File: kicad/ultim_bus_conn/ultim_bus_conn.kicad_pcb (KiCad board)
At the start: 2 copper layers, 121.9 x 10.2 mm, 16 parts, among them P1 CONN_1, P2 CONN_1, P3 CONN_1, P4 CONN_1, P5 CONN_1, P6 CONN_1, P7 CONN_1, P8 CONN_1

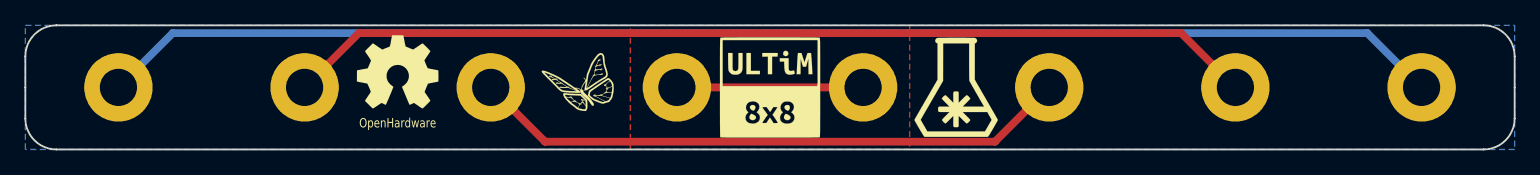
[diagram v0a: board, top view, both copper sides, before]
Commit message: U88 connector strip PCB update
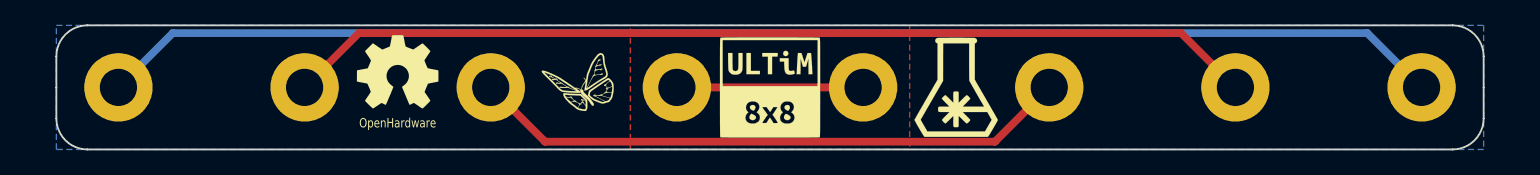
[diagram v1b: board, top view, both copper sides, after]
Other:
- board size 121.9 x 10.2 mm -> 116.8 x 10.2 mm
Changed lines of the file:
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@@
-(kicad_pcb (version 4) (host pcbnew 4.0.6-e0-6349~53~ubuntu16.04.1)
+(kicad_pcb (version 4) (host pcbnew 4.0.7-e0-6372~58~ubuntu16.04.1)
   (general
-    (links 0)
+    (links 4)
     (no_connects 0)
-    (area 43.104999 45.644999 165.175001 55.955001)
+    (area 33.357144 43.7896 162.635001 62.39)
     (thickness 1.6)
     (drawings 12)
@@
     (visible_elements FFFFFF7F)
     (pcbplotparams
-      (layerselection 0x00130_80000001)
-      (usegerberextensions false)
-      (excludeedgelayer false)
+      (layerselection 0x010f0_80000001)
+      (usegerberextensions true)
+      (usegerberattributes true)
+      (excludeedgelayer true)
       (linewidth 0.050800)
-      (plotframeref true)
+      (plotframeref false)
       (viasonmask false)
       (mode 1)
@@
       (plotvalue true)
       (plotinvisibletext false)
-      (padsonsilk true)
-      (subtractmaskfromsilk false)
-      (outputformat 4)
+      (padsonsilk false)
+      (subtractmaskfromsilk true)
+      (outputformat 1)
       (mirror false)
       (drillshape 0)
       (scaleselection 1)
-      (outputdirectory ultim_bus_conn_pdf/))
+      (outputdirectory ultim_bus_conn_gerber/))
   )
   (net 0 "")
@@
     (arrow2b (pts (xy 38.100001 45.72) (xy 38.686422 46.846504)))
   )
-  (dimension 121.92 (width 0.3) (layer Dwgs.User)
-    (gr_text "4.8000 in" (at 104.14 61.039999) (layer Dwgs.User)
+  (dimension 116.84 (width 0.3) (layer Dwgs.User)
+    (gr_text "4.6000 in" (at 104.14 61.039999) (layer Dwgs.User)
       (effects (font (size 1.5 1.5) (thickness 0.3)))
     )
-    (feature1 (pts (xy 165.1 57.15) (xy 165.1 62.389999)))
-    (feature2 (pts (xy 43.18 57.15) (xy 43.18 62.389999)))
-    (crossbar (pts (xy 43.18 59.689999) (xy 165.1 59.689999)))
-    (arrow1a (pts (xy 165.1 59.689999) (xy 163.973496 60.27642)))
-    (arrow1b (pts (xy 165.1 59.689999) (xy 163.973496 59.103578)))
-    (arrow2a (pts (xy 43.18 59.689999) (xy 44.306504 60.27642)))
-    (arrow2b (pts (xy 43.18 59.689999) (xy 44.306504 59.103578)))
-  )
-  (gr_arc (start 162.56 53.34) (end 165.1 53.34) (angle 90) (layer Edge.Cuts) (width 0.15))
-  (gr_arc (start 162.56 48.26) (end 162.56 45.72) (angle 90) (layer Edge.Cuts) (width 0.15))
-  (gr_arc (start 45.72 53.34) (end 45.72 55.88) (angle 90) (layer Edge.Cuts) (width 0.15))
-  (gr_arc (start 45.72 48.26) (end 43.18 48.26) (angle 90) (layer Edge.Cuts) (width 0.15))
-  (gr_line (start 43.18 53.34) (end 43.18 50.8) (layer Edge.Cuts) (width 0.15))
-  (gr_line (start 162.56 55.88) (end 45.72 55.88) (layer Edge.Cuts) (width 0.15))
-  (gr_line (start 165.1 50.8) (end 165.1 53.34) (layer Edge.Cuts) (width 0.15))
-  (gr_line (start 165.1 48.26) (end 165.1 50.8) (layer Edge.Cuts) (width 0.15))
-  (gr_line (start 45.72 45.72) (end 162.56 45.72) (layer Edge.Cuts) (width 0.15))
-  (gr_line (start 43.18 50.8) (end 43.18 48.26) (layer Edge.Cuts) (width 0.15))
+    (feature1 (pts (xy 162.56 57.15) (xy 162.56 62.389999)))
+    (feature2 (pts (xy 45.72 57.15) (xy 45.72 62.389999)))
+    (crossbar (pts (xy 45.72 59.689999) (xy 162.56 59.689999)))
+    (arrow1a (pts (xy 162.56 59.689999) (xy 161.433496 60.27642)))
+    (arrow1b (pts (xy 162.56 59.689999) (xy 161.433496 59.103578)))
+    (arrow2a (pts (xy 45.72 59.689999) (xy 46.846504 60.27642)))
+    (arrow2b (pts (xy 45.72 59.689999) (xy 46.846504 59.103578)))
+  )
+  (gr_arc (start 160.02 53.34) (end 162.56 53.34) (angle 90) (layer Edge.Cuts) (width 0.15))
+  (gr_arc (start 160.02 48.26) (end 160.02 45.72) (angle 90) (layer Edge.Cuts) (width 0.15))
+  (gr_arc (start 48.26 53.34) (end 48.26 55.88) (angle 90) (layer Edge.Cuts) (width 0.15))
+  (gr_arc (start 48.26 48.26) (end 45.72 48.26) (angle 90) (layer Edge.Cuts) (width 0.15))
+  (gr_line (start 45.72 53.34) (end 45.72 50.8) (layer Edge.Cuts) (width 0.15))
+  (gr_line (start 160.02 55.88) (end 48.26 55.88) (layer Edge.Cuts) (width 0.15))
+  (gr_line (start 162.56 50.8) (end 162.56 53.34) (layer Edge.Cuts) (width 0.15))
+  (gr_line (start 162.56 48.26) (end 162.56 50.8) (layer Edge.Cuts) (width 0.15))
+  (gr_line (start 48.26 45.72) (end 160.02 45.72) (layer Edge.Cuts) (width 0.15))
+  (gr_line (start 45.72 50.8) (end 45.72 48.26) (layer Edge.Cuts) (width 0.15))
   (segment (start 50.8 50.8) (end 55.245 46.355) (width 0.635) (layer B.Cu) (net 1))
   (segment (start 55.245 46.355) (end 153.035 46.355) (width 0.635) (layer B.Cu) (net 1))
@@
     (polygon
       (pts
-        (xy 43.18 45.72) (xy 165.1 45.72) (xy 165.1 55.88) (xy 43.18 55.88)
+        (xy 45.72 45.72) (xy 162.56 45.72) (xy 162.56 55.88) (xy 45.72 55.88)
       )
     )
